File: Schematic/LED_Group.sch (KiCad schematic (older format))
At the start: 24 parts, among them Q301 2N2222, U301 TSOP32138

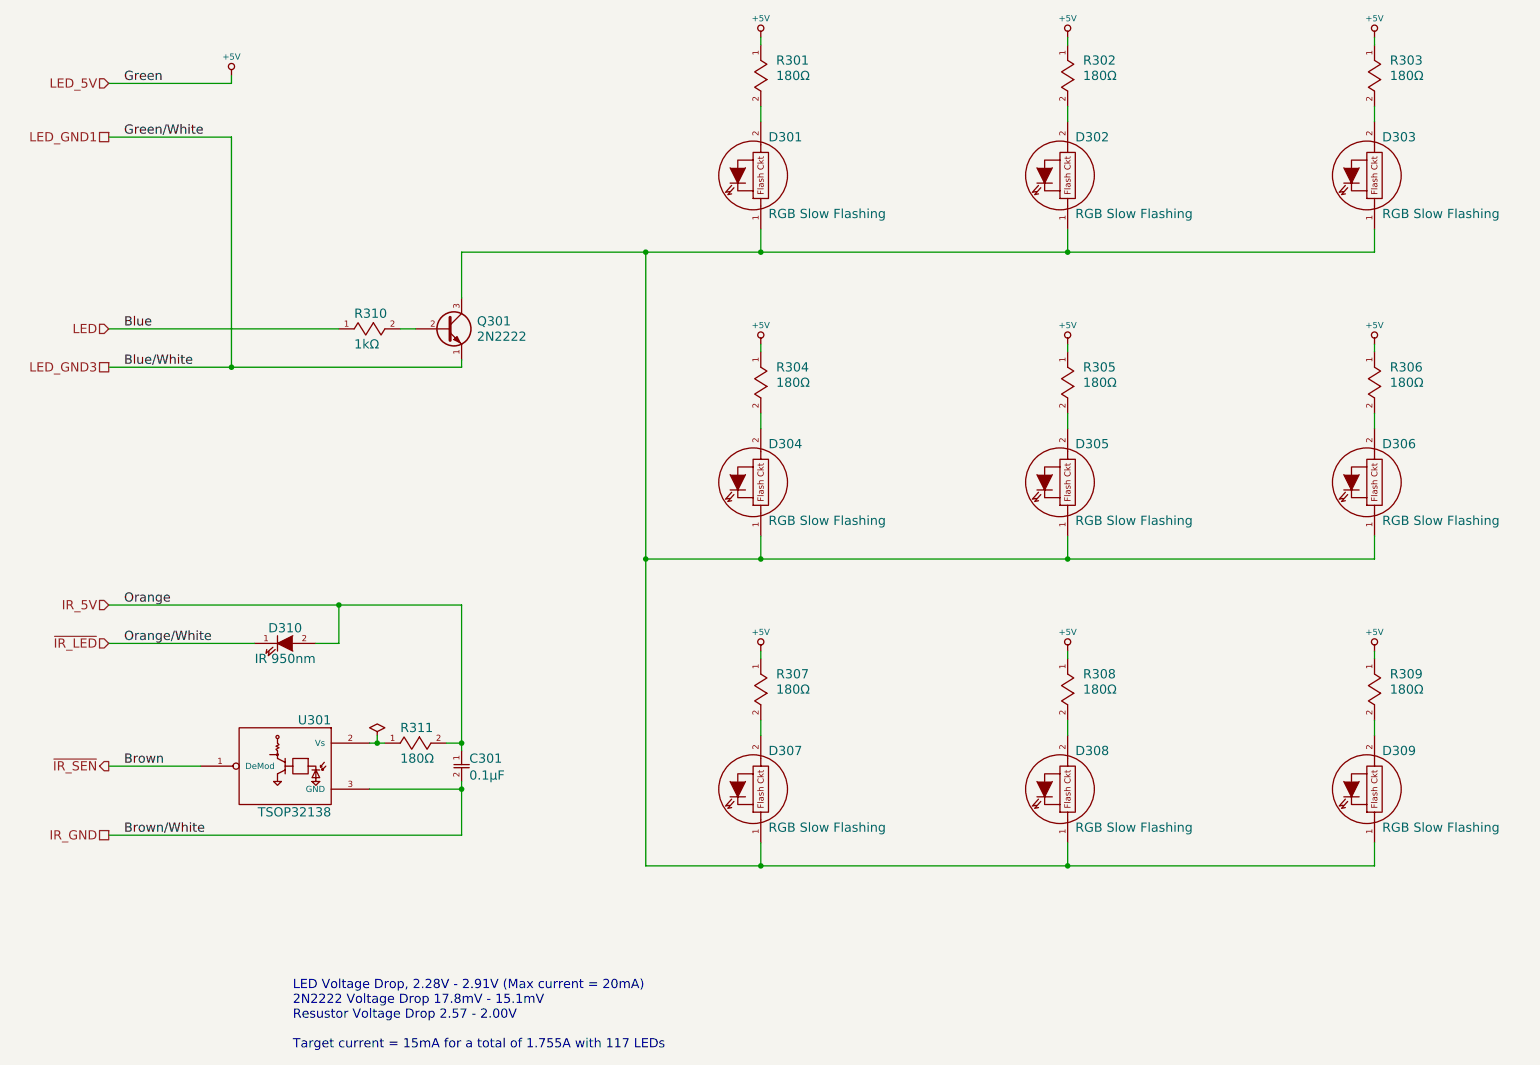
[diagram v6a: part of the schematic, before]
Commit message: Schematic v1.2.4 - Change all 2N2222 BJT to VN3205 N-MOSFET (and remove base/gate resistors.) CyclingRainbow.ino v0.1.1 - Incorporate code from CyclingLEDTimingTest.ino and remove single-switch logic. Ready for first load into prototype hardware.
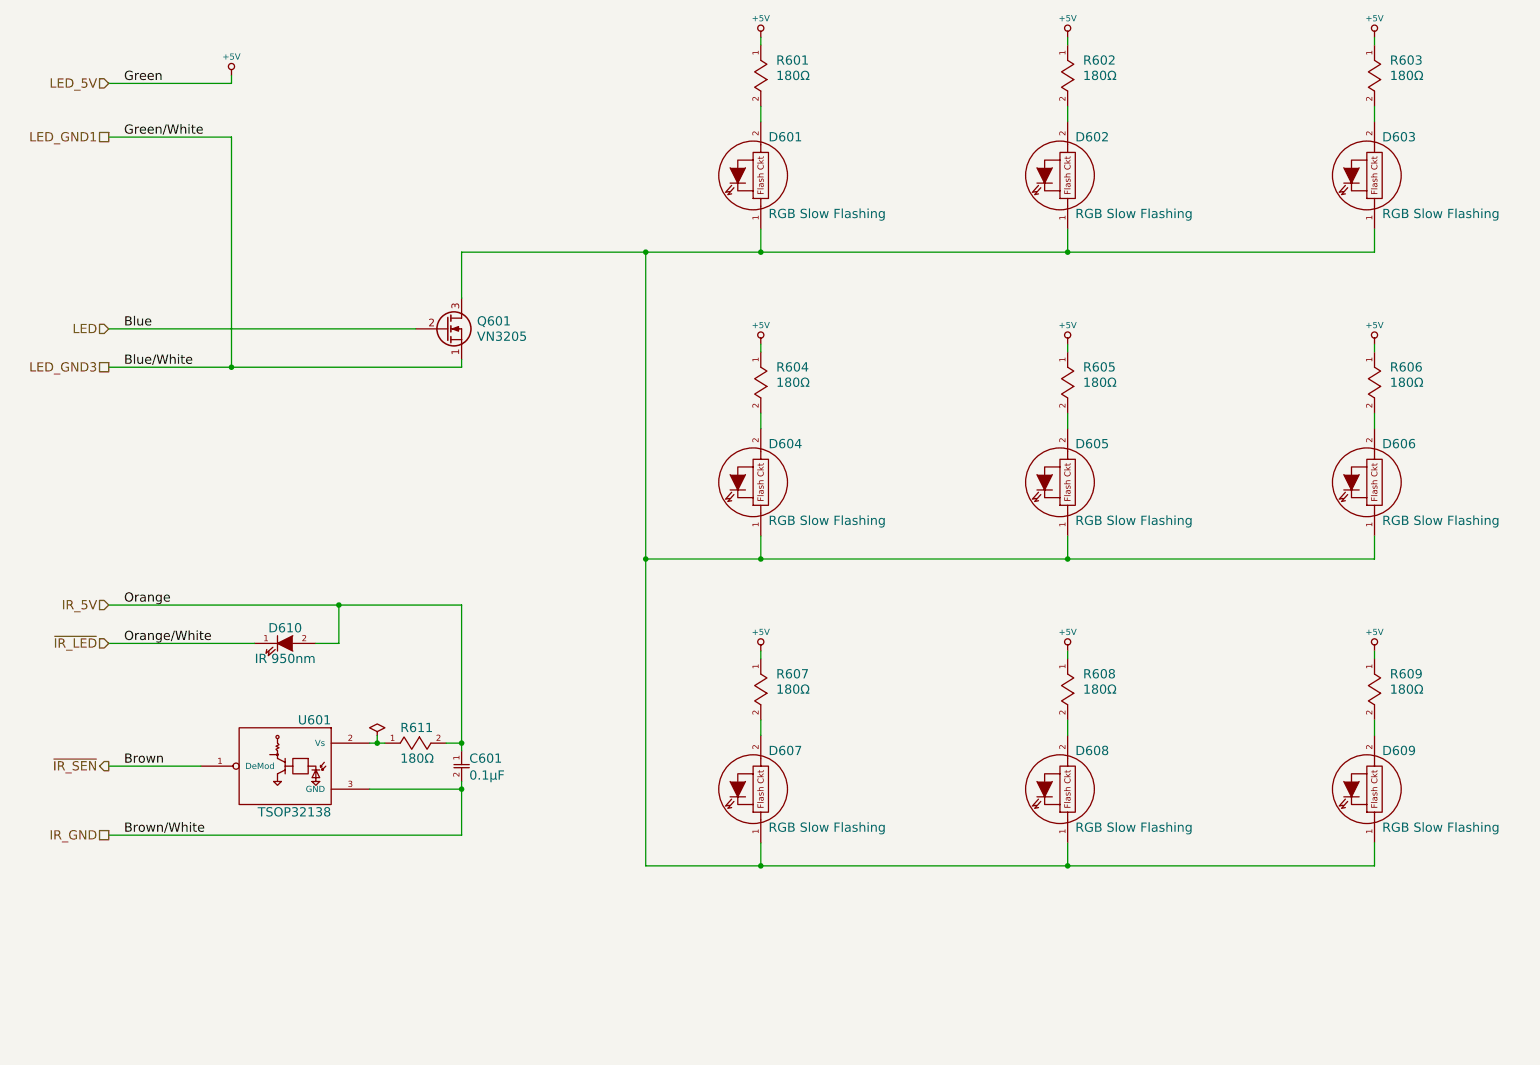
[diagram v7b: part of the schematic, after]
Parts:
- removed Q301: 2N2222, symbol Q_NPN_EBC
- removed R310: 1kΩ, symbol RES
- added Q301: VN3205, TO_SOT_Packages_THT:TO-92_Inline_Wide, symbol Q_NMOS_SGD
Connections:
- net LED: now also Q301.2 (G)
- net LED_GND1: now also Q301.1 (S)
- net at D301.1 (K), D302.1 (K), D303.1 (K)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: now also Q301.3 (D)
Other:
- note removed: "LED Voltage Drop, 2.28V - 2.91V (Max current = 20mA)\n2N2222 Voltage Drop 17.8mV - 15.1mV\nResustor Voltage Drop 2.57 - 2.00V\n\nTarget current = 15mA for a total of 1.755A with 117 LEDs"
